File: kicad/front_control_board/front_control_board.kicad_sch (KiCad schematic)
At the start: 60 parts, among them J1 MAIN_BOARD, J2 DISPLAY, J3 I2C, J4 LED_OUT, Q1 DMN63D8LW, SW1 PEC11R-4215K-S0024, SW2 BTN1, SW3 BTN4, SW4 BTN2, SW5 BTN3, U1 ESP32-WROOM-32UE

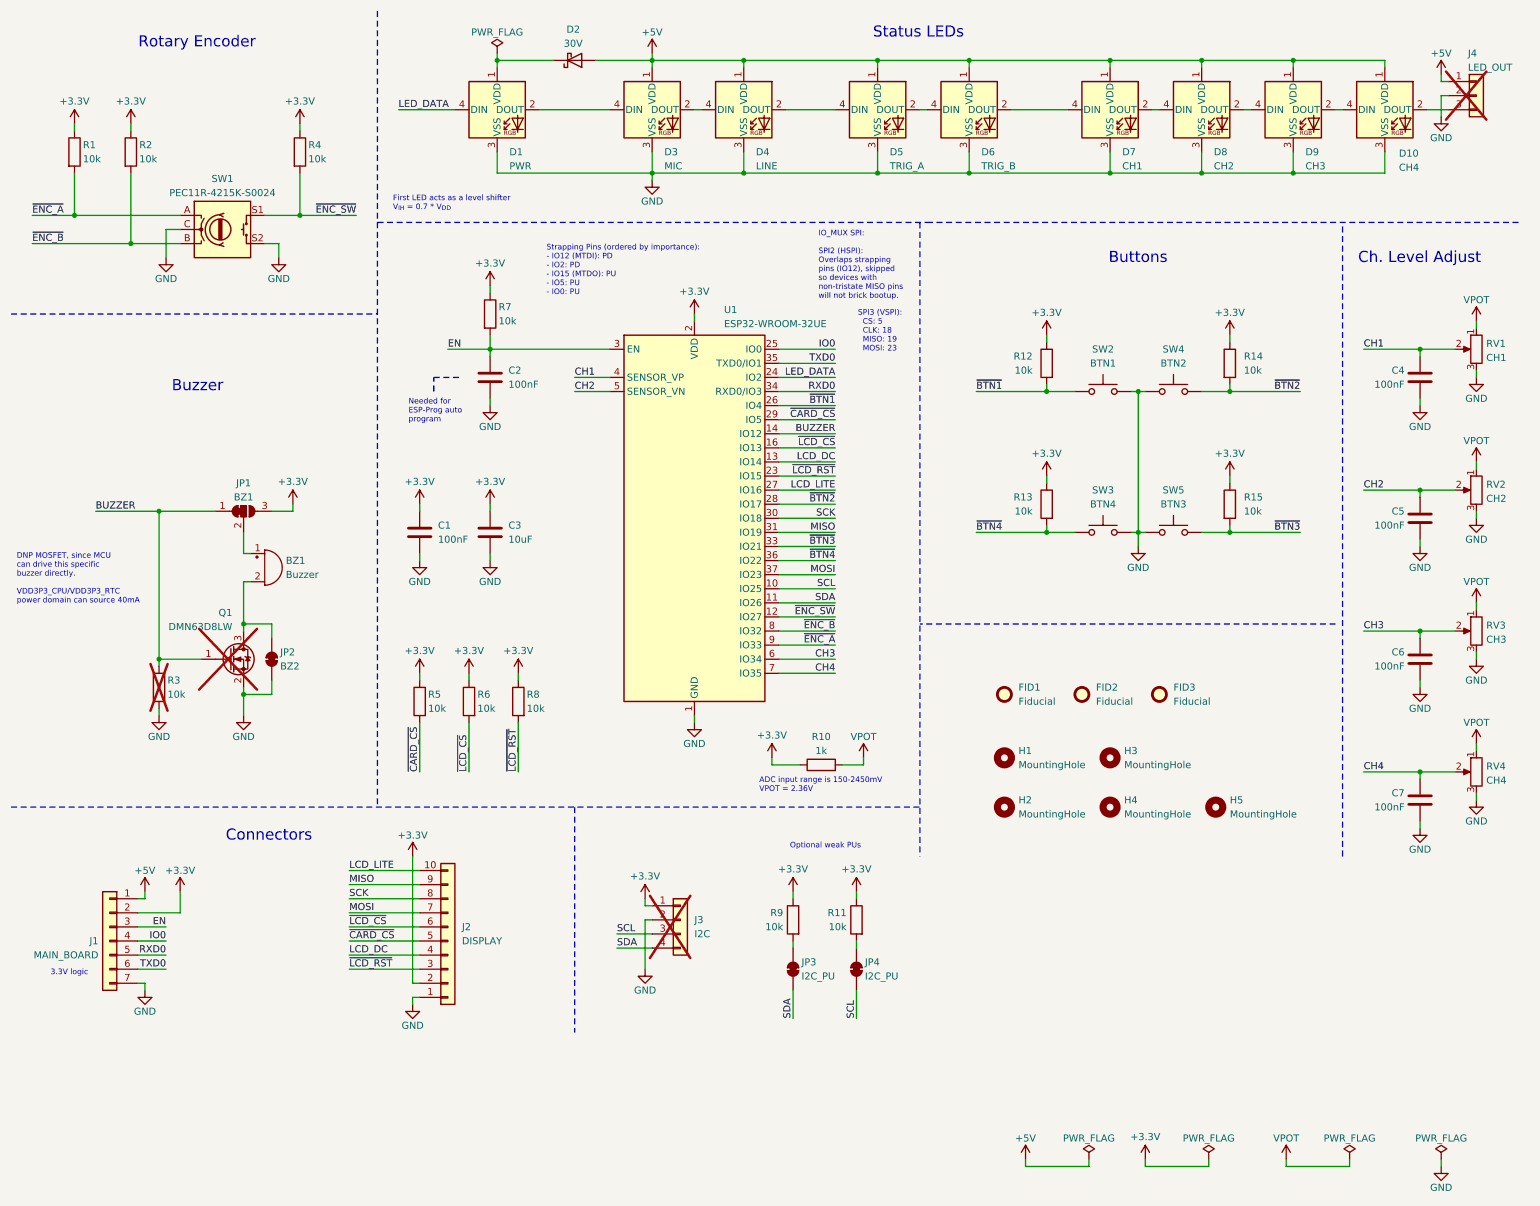
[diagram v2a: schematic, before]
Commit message: add I2S link
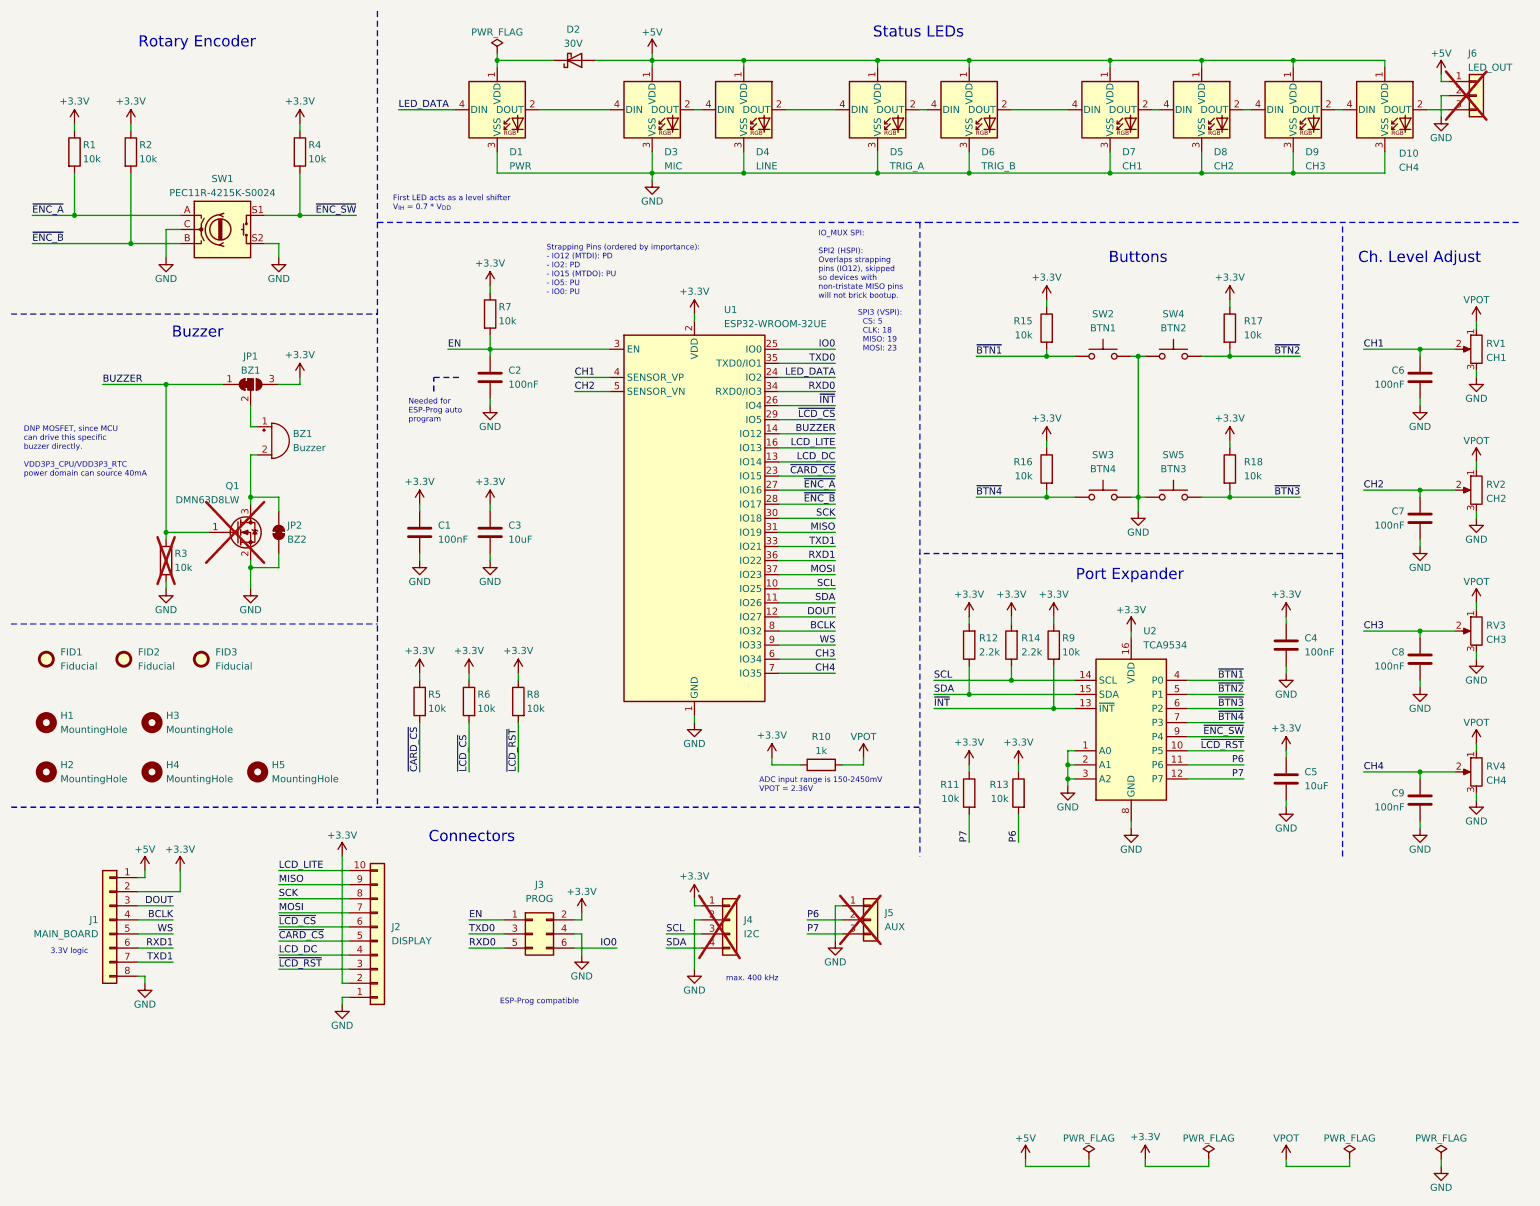
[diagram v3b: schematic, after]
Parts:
- removed JP3, JP4: I2C_PU, Jumper:SolderJumper-2_P1.3mm_Bridged_RoundedPad1.0x1.5mm, symbol Jumper:SolderJumper_2_Bridged
- added C4: 100nF, Capacitor_SMD:C_0603_1608Metric, symbol Device:C
- added C5: 10uF, Capacitor_SMD:C_0603_1608Metric, symbol Device:C
- added J3: PROG, Connector_IDC:IDC-Header_2x03_P2.54mm_Vertical, symbol Connector_Generic:Conn_02x03_Odd_Even
- added J5: AUX, Connector_PinHeader_2.54mm:PinHeader_1x03_P2.54mm_Vertical, symbol Connector_Generic:Conn_01x03
- added R12, R14: 2.2k, Resistor_SMD:R_0603_1608Metric, symbol Device:R
- added R13: 10k, Resistor_SMD:R_0603_1608Metric, symbol Device:R
- added U2: TCA9534, Package_SO:TSSOP-16_4.4x5mm_P0.65mm, symbol Interface_Expansion:TCA9534
- J1: footprint Connector_JST:JST_PH_B8B-PH-K_1x07_P2.00mm_Vertical -> Connector_JST:JST_PH_B8B-PH-K_1x08_P2.00mm_Vertical; symbol Connector_Generic:Conn_01x07 -> Connector_Generic:Conn_01x08
- renumbered C4 to C6, C5 to C7, C6 to C8, C7 to C9, J3 to J4, J4 to J6, R12 to R15, R13 to R16, R14 to R17, R15 to R18
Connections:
- net +3.3V: now also C4.1, C5.1, J3.2 (Pin_2), R12.2, R13.1, R14.2, U2.16 (VDD)
- net EN: now also J3.1 (Pin_1); no longer J1.3 (Pin_3)
- net GND: now also J1.8 (Pin_8), C4.2, C5.2, J3.4 (Pin_4), J5.1 (Pin_1), U2.1 (A0), U2.2 (A1), U2.3 (A2), U2.8 (GND); no longer J1.7 (Pin_7)
- net IO0: now also J3.6 (Pin_6); no longer J1.4 (Pin_4)
- net LCD_LITE: now also U1.16 (IO13); no longer U1.27 (IO16)
- net RXD0: now also J3.5 (Pin_5); no longer J1.5 (Pin_5)
- net SCL: now also R14.1, U2.14 (SCL)
- net SDA: now also R12.1, U2.15 (SDA)
- net TXD0: now also J3.3 (Pin_3); no longer J1.6 (Pin_6)
- net ~{BTN1}: now also U2.4 (P0); no longer U1.26 (IO4)
- net ~{BTN2}: now also U2.5 (P1); no longer U1.28 (IO17)
- net ~{BTN3}: now also U2.6 (P2); no longer U1.33 (IO21)
- net ~{BTN4}: now also U2.7 (P3); no longer U1.36 (IO22)
- net ~{CARD_CS}: now also U1.23 (IO15); no longer U1.29 (IO5)
- net ~{ENC_A}: now also U1.27 (IO16); no longer U1.9 (IO33)
- net ~{ENC_B}: now also U1.28 (IO17); no longer U1.8 (IO32)
- net ~{ENC_SW}: now also U2.9 (P4); no longer U1.12 (IO27)
- net ~{LCD_CS}: now also U1.29 (IO5); no longer U1.16 (IO13)
- net ~{LCD_RST}: now also U2.10 (P5); no longer U1.23 (IO15)
- net ~{INT}: now reaches R9.2
- net ~{INT}: now also U1.26 (IO4), U2.13 (~{INT})
- net P7: now reaches R11.2
- net P7: now also J5.3 (Pin_3), U2.12 (P7)
- new net BCLK: J1.4 (Pin_4), U1.8 (IO32)
- new net DOUT: J1.3 (Pin_3), U1.12 (IO27)
- new net P6: J5.2 (Pin_2), R13.2, U2.11 (P6)
- new net RXD1: J1.6 (Pin_6), U1.36 (IO22)
- new net TXD1: J1.7 (Pin_7), U1.33 (IO21)
- new net WS: J1.5 (Pin_5), U1.9 (IO33)
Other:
- note added: "ESP-Prog compatible"
- note added: "Port Expander"
- note added: "max. 400 kHz"
- note removed: "Optional weak PUs"
- moved on the sheet: BZ1, FID1, FID2, FID3, H1, H2, H3, H4, H5, J2, J4, JP1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

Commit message: remove old part number
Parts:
- SW2, SW3, SW4, SW5: footprint SaawLib:D6C -> (none); MOUSER 611-D6C90F2LFS -> (none); MPN D6C90F2LFS -> (none)
- renumbered R12 to R10, R14 to R12, R15 to R14, R16 to R15, R9 to R16, R10 to R9
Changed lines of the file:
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@@
 		(on_board yes)
 		(dnp no)
-		(property "Reference" "#PWR041"
+		(property "Reference" "#PWR040"
 			(at 199.39 93.98 0)
 			(effects
@@
 			(project "front_control_board"
 				(path "/8a354ba6-ef3b-41b0-9dd3-7bbc957de37e"
-					(reference "#PWR041")
+					(reference "#PWR040")
 					(unit 1)
 				)
@@
 		(on_board yes)
 		(dnp no)
-		(property "Reference" "#PWR027"
+		(property "Reference" "#PWR026"
 			(at 128.27 49.53 0)
 			(effects
@@
 			(project "front_control_board"
 				(path "/8a354ba6-ef3b-41b0-9dd3-7bbc957de37e"
-					(reference "#PWR027")
+					(reference "#PWR026")
 					(unit 1)
 				)
@@
 		(on_board yes)
 		(dnp no)
-		(property "Reference" "#PWR025"
+		(property "Reference" "#PWR024"
 			(at 115.57 189.23 0)
 			(effects
@@
 			(project "front_control_board"
 				(path "/8a354ba6-ef3b-41b0-9dd3-7bbc957de37e"
-					(reference "#PWR025")
+					(reference "#PWR024")
 					(unit 1)
 				)
@@
 		(on_board yes)
 		(dnp no)
-		(property "Reference" "#PWR040"
+		(property "Reference" "#PWR039"
 			(at 199.39 68.58 0)
 			(effects
@@
 			(project "front_control_board"
 				(path "/8a354ba6-ef3b-41b0-9dd3-7bbc957de37e"
-					(reference "#PWR040")
+					(reference "#PWR039")
 					(unit 1)
 				)
@@
 		(on_board yes)
 		(dnp no)
-		(property "Reference" "#PWR026"
+		(property "Reference" "#PWR025"
 			(at 128.27 24.13 0)
 			(effects
@@
 			(project "front_control_board"
 				(path "/8a354ba6-ef3b-41b0-9dd3-7bbc957de37e"
-					(reference "#PWR026")
+					(reference "#PWR025")
 					(unit 1)
 				)
@@
 		(on_board yes)
 		(dnp no)
-		(property "Reference" "R9"
+		(property "Reference" "R16"
 			(at 202.184 125.73 0)
 			(effects
@@
 			(project "front_control_board"
 				(path "/8a354ba6-ef3b-41b0-9dd3-7bbc957de37e"
-					(reference "R9")
+					(reference "R16")
 					(unit 1)
 				)
@@
 		(on_board yes)
 		(dnp no)
-		(property "Reference" "#PWR033"
+		(property "Reference" "#PWR032"
 			(at 161.29 186.69 0)
 			(effects
@@
 			(project "front_control_board"
 				(path "/8a354ba6-ef3b-41b0-9dd3-7bbc957de37e"
-					(reference "#PWR033")
+					(reference "#PWR032")
 					(unit 1)
 				)
@@
 		(on_board yes)
 		(dnp no)
-		(property "Reference" "#PWR036"
+		(property "Reference" "#PWR034"
 			(at 185.42 125.73 0)
 			(effects
@@
 			(project "front_control_board"
 				(path "/8a354ba6-ef3b-41b0-9dd3-7bbc957de37e"
-					(reference "#PWR036")
+					(reference "#PWR034")
 					(unit 1)
 				)
@@
 		(on_board yes)
 		(dnp no)
-		(property "Reference" "#PWR023"
+		(property "Reference" "#PWR041"
 			(at 200.66 125.73 0)
 			(effects
@@
 			(project "front_control_board"
 				(path "/8a354ba6-ef3b-41b0-9dd3-7bbc957de37e"
-					(reference "#PWR023")
+					(reference "#PWR041")
 					(unit 1)
 				)
@@
 		(dnp no)
 		(fields_autoplaced yes)
-		(property "Reference" "R15"
+		(property "Reference" "R14"
 			(at 196.85 68.5799 0)
 			(effects
@@
 			(project "front_control_board"
 				(path "/8a354ba6-ef3b-41b0-9dd3-7bbc957de37e"
-					(reference "R15")
+					(reference "R14")
 					(unit 1)
 				)
@@
 		(on_board yes)
 		(dnp no)
-		(property "Reference" "#PWR029"
+		(property "Reference" "#PWR028"
 			(at 135.89 147.32 0)
 			(effects
@@
 			(project "front_control_board"
 				(path "/8a354ba6-ef3b-41b0-9dd3-7bbc957de37e"
-					(reference "#PWR029")
+					(reference "#PWR028")
 					(unit 1)
 				)
@@
 			)
 		)
-		(property "Footprint" "SaawLib:D6C"
+		(property "Footprint" ""
 			(at 209.55 69.85 0)
 			(effects
@@
 			)
 		)
-		(property "Datasheet" "https://www.ckswitches.com/media/1341/d6.pdf"
+		(property "Datasheet" ""
 			(at 209.55 69.85 0)
 			(effects
@@
 			)
 		)
-		(property "MOUSER" "611-D6C90F2LFS"
+		(property "MOUSER" ""
 			(at 209.55 74.93 0)
 			(effects
@@
 			)
 		)
-		(property "MPN" "D6C90F2LFS "
+		(property "MPN" ""
 			(at 209.55 74.93 0)
 			(effects
@@
 		(on_board yes)
 		(dnp no)
-		(property "Reference" "R14"
+		(property "Reference" "R12"
 			(at 194.818 125.73 0)
 			(effects
@@
 			(project "front_control_board"
 				(path "/8a354ba6-ef3b-41b0-9dd3-7bbc957de37e"
-					(reference "R14")
+					(reference "R12")
 					(unit 1)
 				)
@@
 		(on_board yes)
 		(dnp no)
-		(property "Reference" "#PWR034"
+		(property "Reference" "#PWR033"
 			(at 166.37 151.13 0)
 			(effects
@@
 			(project "front_control_board"
 				(path "/8a354ba6-ef3b-41b0-9dd3-7bbc957de37e"
-					(reference "#PWR034")
+					(reference "#PWR033")
 					(unit 1)
 				)
@@
 		(on_board yes)
 		(dnp no)
-		(property "Reference" "#PWR032"
+		(property "Reference" "#PWR031"
 			(at 149.86 151.13 0)
 			(effects
@@
 			(project "front_control_board"
 				(path "/8a354ba6-ef3b-41b0-9dd3-7bbc957de37e"
-					(reference "#PWR032")
+					(reference "#PWR031")
 					(unit 1)
 				)
@@
 			)
 		)
-		(property "Footprint" "SaawLib:D6C"
+		(property "Footprint" ""
 			(at 222.25 95.25 0)
 			(effects
@@
 			)
 		)
-		(property "Datasheet" "https://www.ckswitches.com/media/1341/d6.pdf"
+		(property "Datasheet" ""
 			(at 222.25 95.25 0)
 			(effects
@@
 			)
 		)
-		(property "MOUSER" "611-D6C90F2LFS"
+		(property "MOUSER" ""
 			(at 222.25 100.33 0)
 			(effects
@@
 			)
 		)
-		(property "MPN" "D6C90F2LFS "
+		(property "MPN" ""
 			(at 222.25 100.33 0)
 			(effects
@@
 			)
 		)
-		(property "Footprint" "SaawLib:D6C"
+		(property "Footprint" ""
 			(at 209.55 95.25 0)
 			(effects
@@
 			)
 		)
-		(property "Datasheet" "https://www.ckswitches.com/media/1341/d6.pdf"
+		(property "Datasheet" ""
 			(at 209.55 95.25 0)
 			(effects
@@
 			)
 		)
-		(property "MOUSER" "611-D6C90F2LFS"
+		(property "MOUSER" ""
 			(at 209.55 100.33 0)
 			(effects
@@
 			)
 		)
-		(property "MPN" "D6C90F2LFS "
+		(property "MPN" ""
 			(at 209.55 100.33 0)
 			(effects
@@
 		(on_board yes)
 		(dnp no)
-		(property "Reference" "#PWR038"
+		(property "Reference" "#PWR036"
 			(at 193.04 125.73 0)
 			(effects
@@
 			(project "front_control_board"
 				(path "/8a354ba6-ef3b-41b0-9dd3-7bbc957de37e"
-					(reference "#PWR038")
+					(reference "#PWR036")
 					(unit 1)
 				)
@@
 		(on_board yes)
 		(dnp no)
-		(property "Reference" "#PWR024"
+		(property "Reference" "#PWR023"
 			(at 115.57 179.07 0)
 			(effects
@@
 			(project "front_control_board"
 				(path "/8a354ba6-ef3b-41b0-9dd3-7bbc957de37e"
-					(reference "#PWR024")
+					(reference "#PWR023")
 					(unit 1)
 				)
@@
 		(on_board yes)
 		(dnp no)
-		(property "Reference" "#PWR039"
+		(property "Reference" "#PWR038"
 			(at 195.58 223.52 0)
 			(effects
@@
 			(project "front_control_board"
 				(path "/8a354ba6-ef3b-41b0-9dd3-7bbc957de37e"
-					(reference "#PWR039")
+					(reference "#PWR038")
 					(unit 1)
 				)
@@
 		(on_board yes)
 		(dnp no)
-		(property "Reference" "R12"
+		(property "Reference" "R10"
 			(at 187.198 125.73 0)
 			(effects
@@
 			(project "front_control_board"
 				(path "/8a354ba6-ef3b-41b0-9dd3-7bbc957de37e"
-					(reference "R12")
+					(reference "R10")
 					(unit 1)
 				)
@@
 		(on_board yes)
 		(dnp no)
-		(property "Reference" "#PWR028"
+		(property "Reference" "#PWR027"
 			(at 135.89 71.12 0)
 			(effects
@@
 			(project "front_control_board"
 				(path "/8a354ba6-ef3b-41b0-9dd3-7bbc957de37e"
-					(reference "#PWR028")
+					(reference "#PWR027")
 					(unit 1)
 				)
@@
 			)
 		)
-		(property "Footprint" "SaawLib:D6C"
+		(property "Footprint" ""
 			(at 222.25 69.85 0)
 			(effects
@@
 			)
 		)
-		(property "Datasheet" "https://www.ckswitches.com/media/1341/d6.pdf"
+		(property "Datasheet" ""
 			(at 222.25 69.85 0)
 			(effects
@@
 			)
 		)
-		(property "MOUSER" "611-D6C90F2LFS"
+		(property "MOUSER" ""
 			(at 222.25 74.93 0)
 			(effects
@@
 			)
 		)
-		(property "MPN" "D6C90F2LFS "
+		(property "MPN" ""
 			(at 222.25 74.93 0)
 			(effects
@@
 		(on_board yes)
 		(dnp no)
-		(property "Reference" "R10"
+		(property "Reference" "R9"
 			(at 158.75 143.51 90)
 			(effects
@@
 			(project "front_control_board"
 				(path "/8a354ba6-ef3b-41b0-9dd3-7bbc957de37e"
-					(reference "R10")
+					(reference "R9")
 					(unit 1)
 				)
@@
 		(on_board yes)
 		(dnp no)
-		(property "Reference" "#PWR031"
+		(property "Reference" "#PWR030"
 			(at 135.89 191.77 0)
 			(effects
@@
 			(project "front_control_board"
 				(path "/8a354ba6-ef3b-41b0-9dd3-7bbc957de37e"
-					(reference "#PWR031")
+					(reference "#PWR030")
 					(unit 1)
 				)
@@
 		(dnp no)
 		(fields_autoplaced yes)
-		(property "Reference" "R16"
+		(property "Reference" "R15"
 			(at 196.85 93.9799 0)
 			(effects
@@
 			(project "front_control_board"
 				(path "/8a354ba6-ef3b-41b0-9dd3-7bbc957de37e"
-					(reference "R16")
+					(reference "R15")
 					(unit 1)
 				)
@@
 		(on_board yes)
 		(dnp no)
-		(property "Reference" "#PWR030"
+		(property "Reference" "#PWR029"
 			(at 135.89 176.53 0)
 			(effects
@@
 			(project "front_control_board"
 				(path "/8a354ba6-ef3b-41b0-9dd3-7bbc957de37e"
-					(reference "#PWR030")
+					(reference "#PWR029")
 					(unit 1)
 				)
